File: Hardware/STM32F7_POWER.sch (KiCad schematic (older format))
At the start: 1 part, among them U5 STM32F765ZGT6

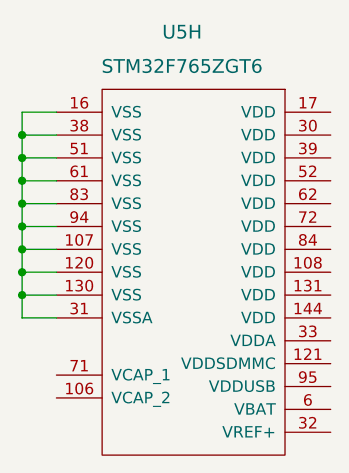
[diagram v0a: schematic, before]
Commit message: Added F0 chip
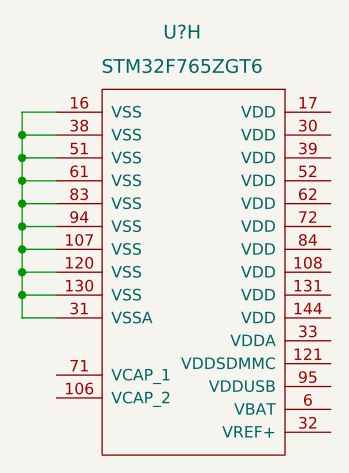
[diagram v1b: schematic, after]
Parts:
- renumbered U5 to U?
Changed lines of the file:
@@
 $Descr A4 11693 8268
 encoding utf-8
-Sheet 17 17
+Sheet 17 18
 Title ""
 Date ""
@@
 P 3350 3150
 AR Path="/5918F046/591902D3" Ref="U?"  Part="8"
-AR Path="/5918F046/59190083/591902D3" Ref="U5"  Part="8"
-F 0 "U5" H 3350 4050 60  0000 C CNN
+AR Path="/5918F046/59190083/591902D3" Ref="U?"  Part="8"
+F 0 "U?" H 3350 4050 60  0000 C CNN
 F 1 "STM32F765ZGT6" H 3350 3900 60  0000 C CNN
 F 2 "" H 4400 3250 60  0001 C CNN

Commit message: Added F7 Circuitry
Added way too much for 1 commit.
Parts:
- gave numbers to parts that had none: 1
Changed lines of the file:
@@
 LIBS:contrib
 LIBS:valves
+LIBS:ZeroPilot-cache
 EELAYER 25 0
 EELAYER END
@@
 Date ""
 Rev ""
-Comp ""
+Comp "WARG"
 Comment1 ""
 Comment2 ""
@@
 P 3350 3150
 AR Path="/5918F046/591902D3" Ref="U?"  Part="8"
-AR Path="/5918F046/59190083/591902D3" Ref="U?"  Part="8"
-F 0 "U?" H 3350 4050 60  0000 C CNN
+AR Path="/5918F046/59190083/591902D3" Ref="U16"  Part="8"
+F 0 "U16" H 3350 4050 60  0000 C CNN
 F 1 "STM32F765ZGT6" H 3350 3900 60  0000 C CNN
 F 2 "" H 4400 3250 60  0001 C CNN
